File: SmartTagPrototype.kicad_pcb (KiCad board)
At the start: 2 copper layers, 12 parts, among them IC1 NRF52810-QFAA-R7, IC3 AEM30940-QFN, X1 32MHz

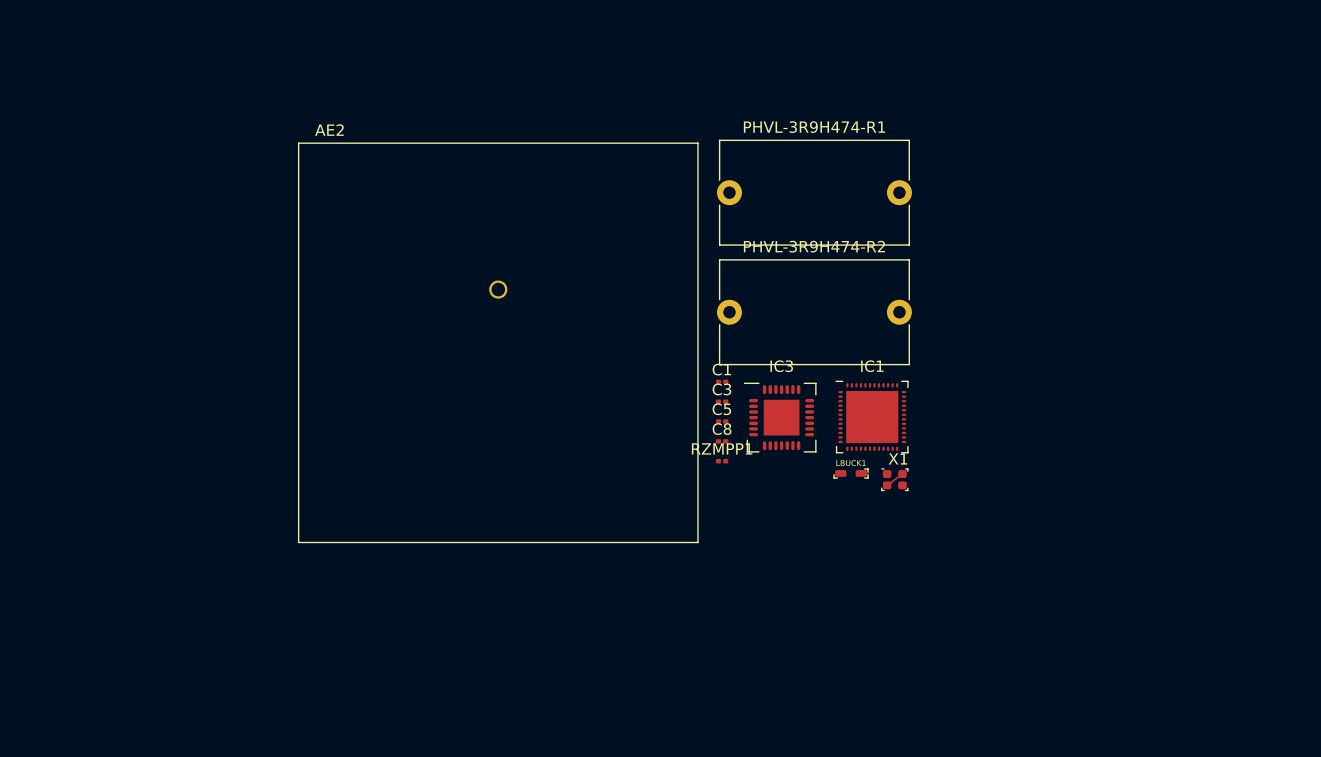
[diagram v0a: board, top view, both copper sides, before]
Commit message: dodanie footprintow do kondensatorow
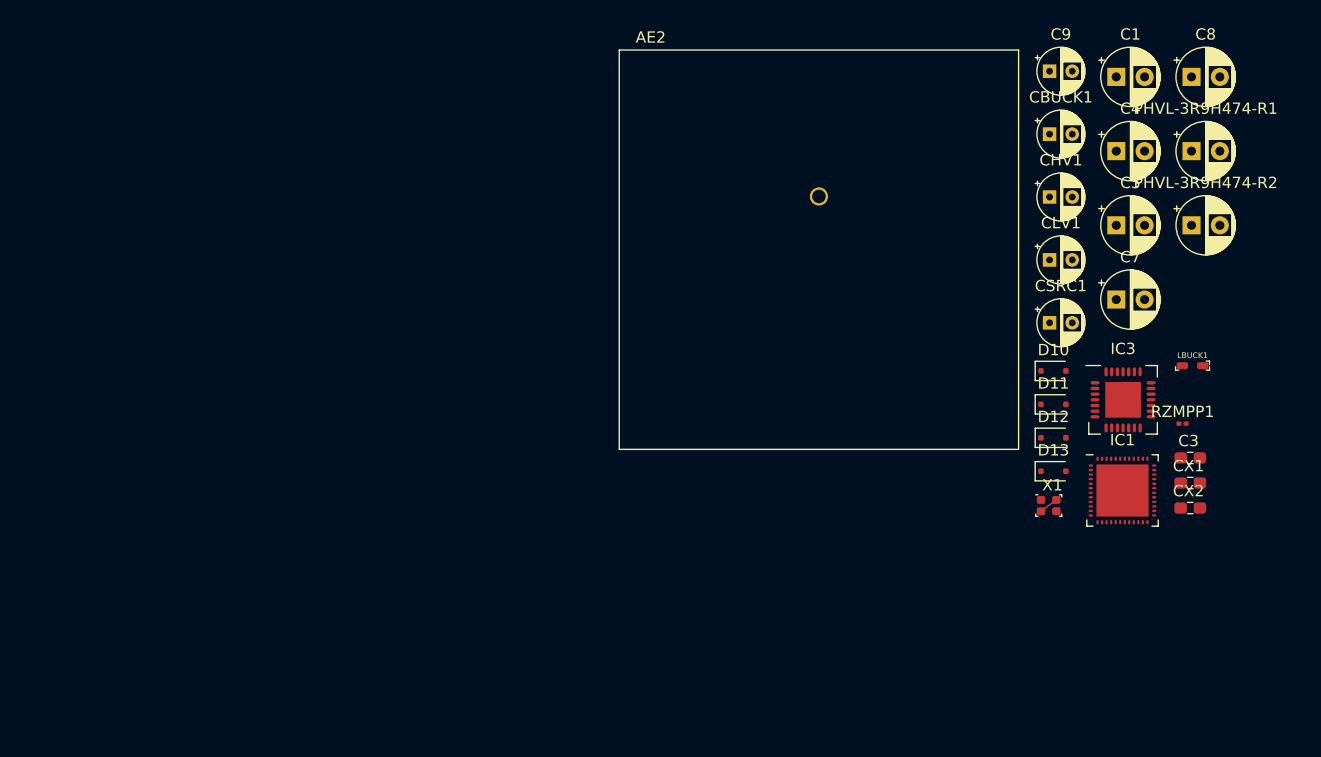
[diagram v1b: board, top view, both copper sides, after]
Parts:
- added C4: 100nF, Capacitor_THT:CP_Radial_D5.0mm_P2.50mm, F.Cu at (178.6, 69.2)
- added C7: 100pF, Capacitor_THT:CP_Radial_D5.0mm_P2.50mm, F.Cu at (178.6, 82.3)
- added C9: 4,7uF, Capacitor_THT:CP_Radial_D4.0mm_P2.00mm, F.Cu at (172.7, 62.2)
- added CBUCK1: 10uF, Capacitor_THT:CP_Radial_D4.0mm_P2.00mm, F.Cu at (172.7, 67.8)
- added CHV1: 10uF, Capacitor_THT:CP_Radial_D4.0mm_P2.00mm, F.Cu at (172.7, 73.3)
- added CLV1: 10uF, Capacitor_THT:CP_Radial_D4.0mm_P2.00mm, F.Cu at (172.7, 78.8)
- added CSRC1: 10uF, Capacitor_THT:CP_Radial_D4.0mm_P2.00mm, F.Cu at (172.7, 84.4)
- added CX1: 12pF, Library:C_2.8x1, F.Cu at (185.0, 98.5)
- added CX2: 12pF, Library:C_2.8x1, F.Cu at (185.0, 100.8)
- added D10: D_Schottky, Diode_SMD:D_SOD-323F, F.Cu at (173.1, 88.7)
- added D11: D_Schottky, Diode_SMD:D_SOD-323F, F.Cu at (173.1, 91.6)
- added D12: D_Schottky, Diode_SMD:D_SOD-323F, F.Cu at (173.1, 94.5)
- added D13: D_Schottky, Diode_SMD:D_SOD-323F, F.Cu at (173.1, 97.5)
- C1, C5, C8: footprint Capacitor_SMD:C_0201_0603Metric -> Capacitor_THT:CP_Radial_D5.0mm_P2.50mm
- C3: footprint Capacitor_SMD:C_0201_0603Metric -> Library:C_2.8x1
- PHVL-3R9H474-R1, PHVL-3R9H474-R2: footprint Capacitor_THT:C_Rect_L16.5mm_W9.0mm_P15.00mm_MKT -> Capacitor_THT:CP_Radial_D5.0mm_P2.50mm
- moved C8 52.4 mm to (185.3, 62.7)
- moved C1 44.0 mm to (178.6, 62.7)
- moved PHVL-3R9H474-R2 41.5 mm to (185.3, 75.8)
- moved C3 41.5 mm to (185.0, 96.3)
- moved PHVL-3R9H474-R1 40.9 mm to (185.3, 69.2)
- moved RZMPP1 40.8 mm to (184.5, 93.3)
- moved C5 38.9 mm to (178.6, 75.8)
- moved LBUCK1 31.6 mm to (185.3, 91.7)
- moved IC3 30.2 mm to (179.2, 91.2)
- moved AE2 29.5 mm to (152.4, 73.2)
- moved IC1 23.0 mm to (179.2, 99.2)
- moved X1 13.8 mm to (172.0, 100.0)

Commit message: dodane gniazda i rezystory, cewki ciagle do zrobienia
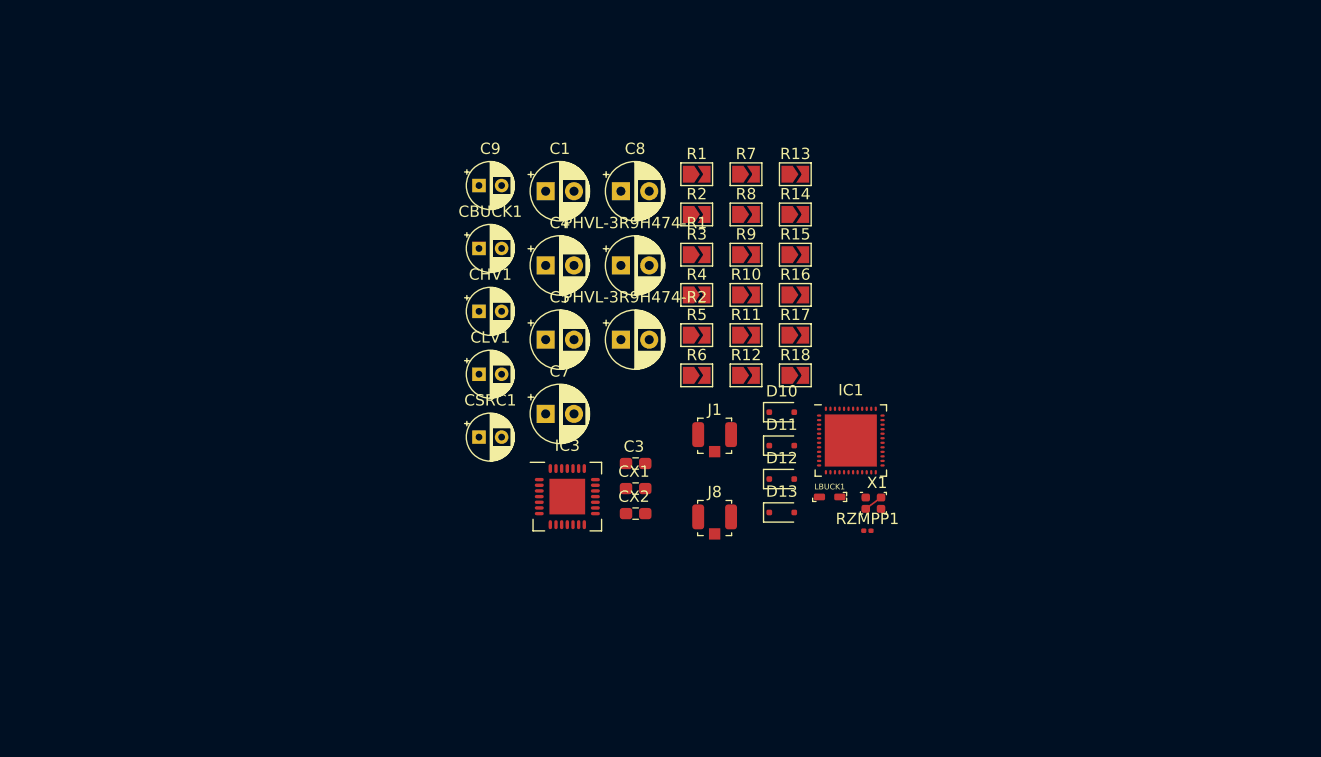
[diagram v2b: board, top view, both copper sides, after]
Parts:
- removed AE2: Antenna, RF_Antenna:Astrocast_AST50127-00
- added J1: Nordic output antenna, Library:U_FL, F.Cu at (143.2, 94.3)
- added J8: Conn_Coaxial, Library:U_FL, F.Cu at (143.2, 101.6)
- added R1: 0, Jumper:SolderJumper-2_P1.3mm_Open_TrianglePad1.0x1.5mm, F.Cu at (141.6, 71.3)
- added R10: 0, Jumper:SolderJumper-2_P1.3mm_Open_TrianglePad1.0x1.5mm, F.Cu at (145.9, 81.9)
- added R11: 0, Jumper:SolderJumper-2_P1.3mm_Open_TrianglePad1.0x1.5mm, F.Cu at (145.9, 85.5)
- added R12: 0, Jumper:SolderJumper-2_P1.3mm_Open_TrianglePad1.0x1.5mm, F.Cu at (145.9, 89.0)
- added R13: 0, Jumper:SolderJumper-2_P1.3mm_Open_TrianglePad1.0x1.5mm, F.Cu at (150.3, 71.3)
- added R14: NC, Jumper:SolderJumper-2_P1.3mm_Open_TrianglePad1.0x1.5mm, F.Cu at (150.3, 74.8)
- added R15: 0, Jumper:SolderJumper-2_P1.3mm_Open_TrianglePad1.0x1.5mm, F.Cu at (150.3, 78.4)
- added R16: 0, Jumper:SolderJumper-2_P1.3mm_Open_TrianglePad1.0x1.5mm, F.Cu at (150.3, 81.9)
- added R17: 0, Jumper:SolderJumper-2_P1.3mm_Open_TrianglePad1.0x1.5mm, F.Cu at (150.3, 85.5)
- added R18: 0, Jumper:SolderJumper-2_P1.3mm_Open_TrianglePad1.0x1.5mm, F.Cu at (150.3, 89.0)
- added R2: 0, Jumper:SolderJumper-2_P1.3mm_Open_TrianglePad1.0x1.5mm, F.Cu at (141.6, 74.8)
- added R3: 0, Jumper:SolderJumper-2_P1.3mm_Open_TrianglePad1.0x1.5mm, F.Cu at (141.6, 78.4)
- added R4: 0, Jumper:SolderJumper-2_P1.3mm_Open_TrianglePad1.0x1.5mm, F.Cu at (141.6, 81.9)
- added R5: 0, Jumper:SolderJumper-2_P1.3mm_Open_TrianglePad1.0x1.5mm, F.Cu at (141.6, 85.5)
- added R6: 0, Jumper:SolderJumper-2_P1.3mm_Open_TrianglePad1.0x1.5mm, F.Cu at (141.6, 89.0)
- added R7: 0, Jumper:SolderJumper-2_P1.3mm_Open_TrianglePad1.0x1.5mm, F.Cu at (145.9, 71.3)
- added R8: 0, Jumper:SolderJumper-2_P1.3mm_Open_TrianglePad1.0x1.5mm, F.Cu at (145.9, 74.8)
- added R9: 0, Jumper:SolderJumper-2_P1.3mm_Open_TrianglePad1.0x1.5mm, F.Cu at (145.9, 78.4)
- moved C1 51.4 mm to (128.3, 72.8)
- moved C4 51.4 mm to (128.3, 79.3)
- moved C5 51.4 mm to (128.3, 85.9)
- moved C7 51.4 mm to (128.3, 92.4)
- moved C8 51.4 mm to (134.9, 72.8)
- moved C9 51.4 mm to (122.4, 72.3)
- moved CBUCK1 51.4 mm to (122.4, 77.8)
- moved CHV1 51.4 mm to (122.4, 83.4)
- moved CLV1 51.4 mm to (122.4, 88.9)
- moved CSRC1 51.4 mm to (122.4, 94.5)
- moved PHVL-3R9H474-R1 51.4 mm to (134.9, 79.3)
- moved PHVL-3R9H474-R2 51.4 mm to (134.9, 85.9)
- moved IC3 49.8 mm to (130.2, 99.7)
- moved C3 48.9 mm to (136.1, 96.8)
- moved CX1 48.9 mm to (136.1, 99.0)
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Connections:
- IC1 pad 11: unconnected-(IC1-P0.09-Pad11) -> Net-(IC1-P0.09)
- IC1 pad 12: unconnected-(IC1-P0.10-Pad12) -> Net-(IC1-P0.10)
- IC1 pad 24: unconnected-(IC1-P0.21/NRESET-Pad24) -> Net-(IC1-P0.21/NRESET)

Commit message: jeszcze kondensator zgubilem, teraz jest WSZYSTKO (punkty testowe kiedy indziej sie zrobi)
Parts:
- added CBOOST1: 22uF, Capacitor_THT:CP_Radial_D4.0mm_P2.00mm, F.Cu at (159.8, 84.7)
- added L1: 3.9nH, Library:SMD_2.0x1.0, F.Cu at (176.5, 110.1)
- added LBOOST1: 10uH, Library:SMD_1.6_1.5, F.Cu at (172.7, 106.8)
- LBUCK1: footprint Library:JELF243A -> Library:SMD_1.6_1.5
- moved IC3 45.0 mm to (175.1, 101.7)
- moved CBUCK1 39.4 mm to (159.8, 90.3)
- moved CHV1 39.4 mm to (159.8, 95.8)
- moved CLV1 39.4 mm to (159.8, 101.4)
- moved CSRC1 39.4 mm to (159.8, 106.9)
- moved C9 38.0 mm to (159.8, 79.2)
- moved D10 33.0 mm to (178.8, 77.9)
- moved D13 33.0 mm to (178.8, 86.7)
- moved D11 33.0 mm to (178.8, 80.8)
- moved D12 33.0 mm to (178.8, 83.8)
- moved R15 25.1 mm to (174.4, 85.3)
- moved R16 25.1 mm to (174.4, 88.8)
- moved R17 25.1 mm to (174.4, 92.4)
- moved R13 25.1 mm to (174.4, 78.2)
- moved R14 25.1 mm to (174.4, 81.7)
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
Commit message: wstępnie poukładane pcb
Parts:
- moved D11 82.3 mm to (104.3, 115.8)
- moved D10 82.3 mm to (104.3, 112.8)
- moved D13 75.8 mm to (108.8, 115.8)
- moved D12 75.8 mm to (108.8, 112.8)
- moved R13 69.9 mm to (108.3, 100.7), turned to 90 degrees
- moved R1 67.5 mm to (103.8, 105.0), turned to 180 degrees
- moved R2 67.5 mm to (103.8, 108.5), turned to 180 degrees
- moved R18 67.3 mm to (108.3, 108.5), turned to 180 degrees
- moved R12 65.7 mm to (104.5, 100.7), turned to 90 degrees
- moved J8 63.0 mm to (106.0, 94.4)
- moved R3 60.7 mm to (108.3, 105.0), turned to 180 degrees
- moved R15 54.6 mm to (120.3, 92.8)
- moved R16 54.6 mm to (120.3, 95.8)
- moved R17 54.5 mm to (120.3, 98.8)
- moved IC3 51.4 mm to (124.2, 108.9)
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
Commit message: sciezki przy aemie / PCB
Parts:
- moved R15 13.5 mm to (117.5, 106.0)
- moved R16 13.5 mm to (117.5, 109.0)
- moved R17 13.5 mm to (117.5, 112.0)
- moved R4 13.3 mm to (112.8, 106.0)
- moved R5 13.3 mm to (112.8, 109.0)
- moved R6 13.3 mm to (112.8, 112.0)
- moved CBOOST1 10.4 mm to (118.0, 100.5)
- moved CSRC1 8.50 mm to (118.0, 94.5), turned to 180 degrees
- moved D12 7.42 mm to (103.0, 117.5), turned to -90 degrees
- moved LBUCK1 6.26 mm to (121.0, 99.0)
- moved LBOOST1 6.04 mm to (121.0, 95.5)
- moved CBUCK1 4.76 mm to (112.0, 116.0), turned to -90 degrees
- moved CHV1 4.10 mm to (122.6, 115.9)
- moved CLV1 4.10 mm to (117.3, 115.9)
- moved D11 3.22 mm to (106.5, 113.5), turned to -90 degrees
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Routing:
- net /VBUCK: track 0.00 -> 55.5 mm, vias 0 -> 8
- net Net-(D10-K): track 0.00 -> 31.1 mm, vias 0 -> 4
- net Net-(D10-A): track 0.00 -> 17.3 mm, vias 0 -> 2
- net Net-(D11-A): track 0.00 -> 16.6 mm
- net Net-(IC3-BUFSRC): track 0.00 -> 16.1 mm
- net Net-(IC3-CFG[2]): track 0.00 -> 11.4 mm
- net Net-(IC3-SWBUCK): track 0.00 -> 10.5 mm
- net Net-(IC3-CFG[0]): track 0.00 -> 10.2 mm
- net Net-(IC3-LVOUT): track 0.00 -> 9.92 mm
- net Net-(IC3-CFG[1]): track 0.00 -> 9.69 mm
- net Net-(IC3-BOOST): track 0.00 -> 9.24 mm, vias 0 -> 1
- net Net-(J8-Ext): track 0.00 -> 8.96 mm
- net Net-(IC1-VDD_1): track 0.00 -> 6.50 mm, vias 0 -> 1
- net Net-(J8-In): track 0.00 -> 4.78 mm

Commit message: przed wylaniem masy / PCB
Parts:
- moved R9 15.5 mm to (137.2, 103.7), turned to 180 degrees
- moved IC1 15.4 mm to (132.0, 97.3)
- moved RZMPP1 14.8 mm to (122.5, 97.2), turned to -90 degrees
- moved PHVL-3R9H474-R1 14.4 mm to (131.4, 105.0), turned to 180 degrees
- moved L1 14.3 mm to (143.3, 107.5)
- moved C9 14.1 mm to (124.5, 110.9), turned to -90 degrees
- moved C3 13.5 mm to (142.9, 105.5)
- moved C1 13.4 mm to (123.0, 90.5)
- moved C7 11.3 mm to (150.4, 102.5)
- moved J1 10.5 mm to (151.4, 112.0), turned to -90 degrees
- moved C4 10.1 mm to (139.4, 91.5)
- moved C5 10.1 mm to (145.2, 91.5)
- moved C8 10.1 mm to (151.2, 91.5)
- moved R10 9.99 mm to (143.4, 99.3)
- moved R11 9.99 mm to (143.4, 95.8)
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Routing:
- net Net-(IC1-VDD_1): track 6.50 -> 46.7 mm, vias 1 -> 4
- net Net-(IC1-DEC3): track 0.00 -> 18.4 mm
- net Net-(PHVL-3R9H474-R1-Pad2): track 0.00 -> 17.5 mm
- net Net-(IC3-BAL): track 0.00 -> 14.6 mm, vias 0 -> 2
- net Net-(IC1-ANT): track 0.00 -> 13.4 mm
- net Net-(IC1-DEC2): track 0.00 -> 12.8 mm
- net Net-(IC1-DEC1): track 0.00 -> 12.5 mm, vias 0 -> 1
- net Net-(X1-XTAL_1): track 0.00 -> 11.4 mm
- net Net-(X1-XTAL_2): track 0.00 -> 10.9 mm
- net Net-(IC1-XC1): track 0.00 -> 10.3 mm
- net Net-(IC3-BATT): track 0.00 -> 9.15 mm
- net Net-(IC1-XC2): track 0.00 -> 9.05 mm
- net Net-(J1-In): track 0.00 -> 7.99 mm
- net Net-(IC1-DEC4): track 0.00 -> 7.88 mm
- net Net-(IC1-P0.08): track 0.00 -> 7.61 mm
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
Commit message: ala gotowe PCB, wylane masy
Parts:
- moved CX1 9.50 mm to (142.7, 96.5)
- moved CX2 9.50 mm to (142.7, 93.8)
- moved R7 9.50 mm to (127.7, 108.5)
- moved C1 9.50 mm to (113.5, 89.5)
- moved C9 9.50 mm to (115.0, 109.9)
- moved CBOOST1 9.50 mm to (105.5, 94.5)
- moved CBUCK1 9.50 mm to (99.5, 110.0)
- moved CHV1 9.50 mm to (110.1, 109.9)
- moved CLV1 9.50 mm to (104.8, 109.9)
- moved CSRC1 9.50 mm to (105.5, 88.5)
- moved D10 9.50 mm to (90.5, 107.5)
- moved D11 9.50 mm to (94.0, 107.5)
- moved D12 9.50 mm to (90.5, 111.5)
- moved D13 9.50 mm to (94.0, 111.5)
- moved IC1 9.50 mm to (122.6, 96.3)
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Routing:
- net GND: track 0.00 -> 13.9 mm, vias 0 -> 6
- net /VBUCK: track 53.8 -> 64.1 mm, vias 11 -> 12
- net Net-(IC1-VDD_1): track 46.7 -> 55.8 mm, vias 4 -> 5
- added copper zone on B.Cu, net GND
- added copper zone on F.Cu, net GND
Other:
- board outline added: 57 x 31 mm

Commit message: push abominacji czytaj dodany footprint i symbol zlacza testowego (niech Bog ma mnie w opiece)
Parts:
- added DIAG1: ~, Library:DIAG, F.Cu at (115.5, 70.7)
- added J7: Additional AC pins, Connector_PinHeader_2.54mm:PinHeader_1x02_P2.54mm_Vertical, F.Cu at (83.5, 69.3)
- added J9: AC pins (generator/antenna), Connector_PinHeader_2.54mm:PinHeader_1x02_P2.54mm_Vertical, F.Cu at (85.0, 80.2)
